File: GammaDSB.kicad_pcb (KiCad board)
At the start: 2 copper layers, 85 x 50 mm, 75 parts, among them J1 AudioIn, J2 AudioOut, J3 Conn_Coaxial, J4 Barrel_Jack, K1 G5V-2, Q1 BC-817, Q2 BC-817, Q3 BC-817, Q4 BC-817, Q5 C1162, Q6 BC817, Q7 BC-817, Q8 BC-817, T1 FT37-43 BIF8T, U1 MCP1700-5002E_SOT89, U2 NE602, Y1 7074, Y2 7074

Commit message: Small improvements.
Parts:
- Q6: value BC817 -> BC807
- moved C25 12.4 mm to (198.2, 108.4), turned to 90 degrees
- moved C10 6.07 mm to (151.7, 111.0), turned to 0 degrees
- moved C5 3.98 mm to (157.3, 109.5), turned to 270 degrees
- moved R17 3.84 mm to (151.2, 118.0), turned to 180 degrees
- moved C14 3.58 mm to (154.2, 98.2), turned to 0 degrees
- moved R21 2.20 mm to (161.6, 117.7)
- moved Y1 2.00 mm to (160.8, 106.0)
- moved R3 1.93 mm to (156.8, 101.0)
- moved D3 1.60 mm to (158.7, 116.0)
- moved C26 1.20 mm to (148.6, 114.2)
- moved Q2 0.40 mm to (154.1, 101.0)
- moved C8 0.36 mm to (157.3, 106.3)
- moved Q6 0.20 mm to (155.6, 117.2)
- moved C28 0.10 mm to (163.3, 114.3)
- moved Q7 0.10 mm to (166.7, 115.1)
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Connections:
- C5 pad 1: Net-(C10-Pad2) -> Net-(C5-Pad1)
- R16 pad 2: Net-(R16-Pad2) -> +12V
- R19 pad 2: Net-(R16-Pad2) -> +12V
- R20 pad 2: Net-(R16-Pad2) -> +12V
- U2 pad 1: Net-(C10-Pad2) -> Net-(C5-Pad1)
- Y1 pad 1: Net-(C10-Pad2) -> Net-(C5-Pad1)
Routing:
- net +12V: track 126.6 -> 168.9 mm
- net Net-(C5-Pad1): track 0.00 -> 7.14 mm
- net Net-(C10-Pad1): track 29.7 -> 23.3 mm
- net Net-(C10-Pad2): track 12.7 -> 7.83 mm
- net Net-(C14-Pad1): track 21.1 -> 16.7 mm
- net Net-(R16-Pad2): track 3.42 -> 0.00 mm
- net Net-(K1-Pad11): track 21.3 -> 23.1 mm
- net Net-(C25-Pad2): track 17.6 -> 19.1 mm
- net /VccR: track 27.5 -> 28.4 mm
- net /VccT: track 49.1 -> 50.0 mm
- net Net-(C28-Pad1): track 58.2 -> 57.4 mm
- net Net-(C28-Pad2): track 6.31 -> 5.63 mm
- net GND: track 78.2 -> 78.1 mm, vias 100 -> 102

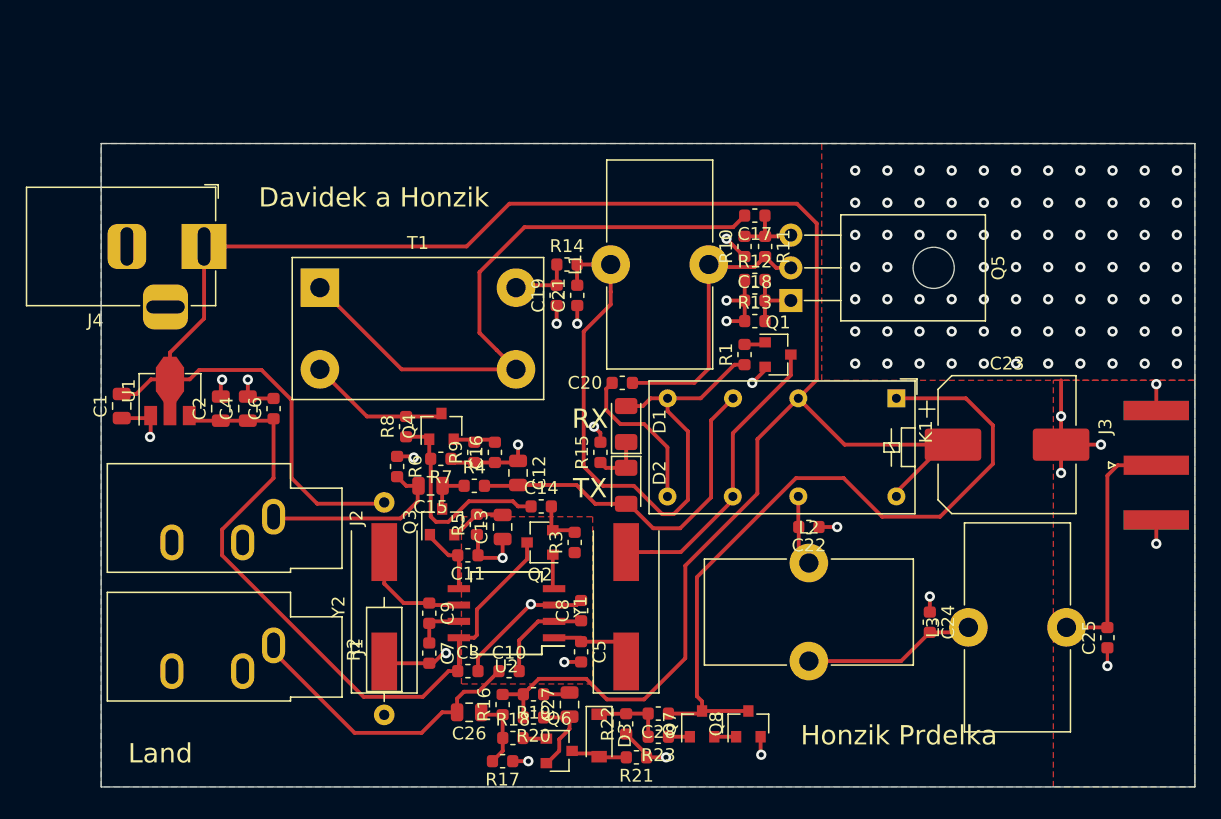
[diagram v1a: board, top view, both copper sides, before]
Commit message: Changed L1 and T1 footprints
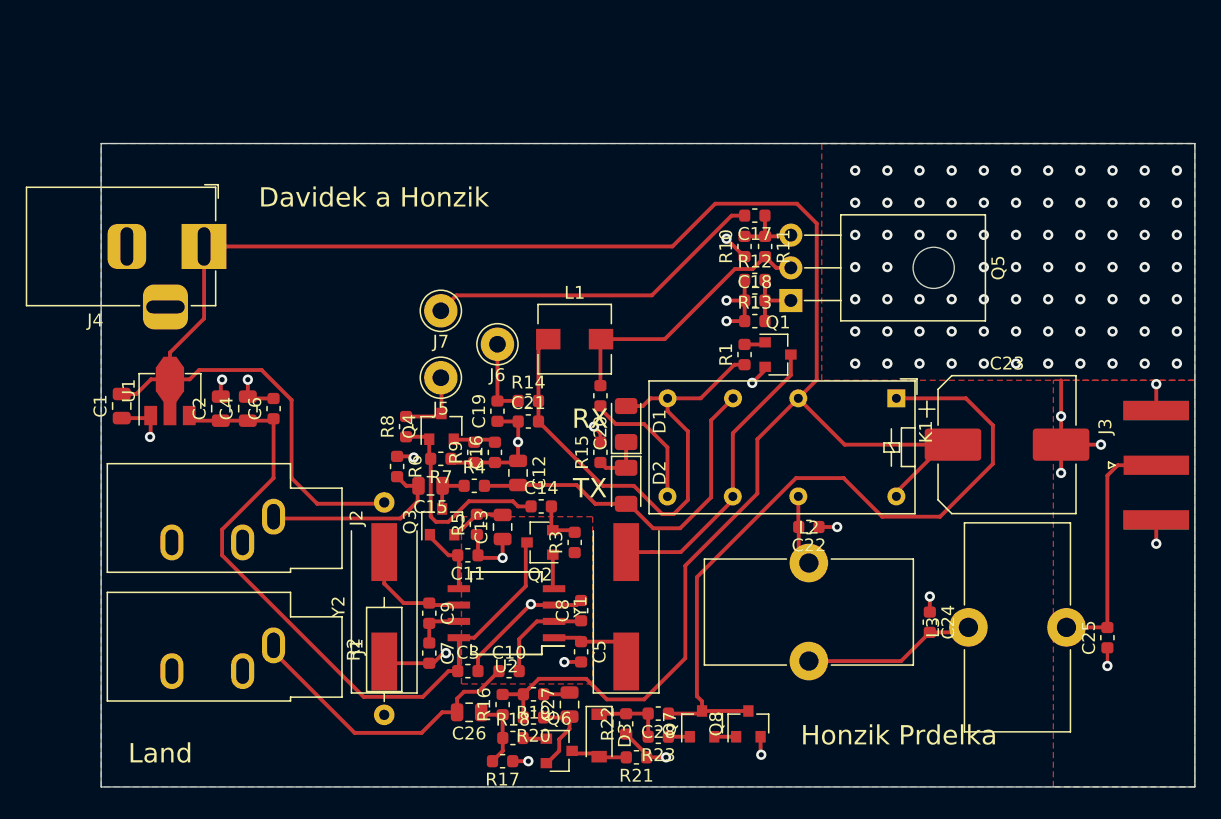
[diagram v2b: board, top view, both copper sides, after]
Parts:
- removed T1: FT37-43 BIF8T, Inductor_THT:L_CommonMode_Toroid_Vertical_L19.3mm_W10.8mm_Px6.35mm_Py15.24mm_Bourns_8100
- added J5: Conn_01x01, Connector_Pin:Pin_D1.3mm_L11.0mm, F.Cu at (146.4, 88.2)
- added J6: Conn_01x01, Connector_Pin:Pin_D1.3mm_L11.0mm, F.Cu at (150.8, 85.6)
- added J7: Conn_01x01, Connector_Pin:Pin_D1.3mm_L11.0mm, F.Cu at (146.4, 83.0)
- L1: value FT37-43 8T -> 74437324220; footprint Inductor_THT:L_Toroid_Vertical_L16.0mm_W8.0mm_P7.62mm -> Inductor_SMD:L_Wuerth_HCI-5040
- moved R14 11.0 mm to (153.2, 90.0)
- moved C21 10.5 mm to (153.2, 91.6), turned to 0 degrees
- moved C19 10.1 mm to (150.8, 90.8)
- moved L1 6.44 mm to (156.8, 85.2), turned to 0 degrees
- moved C20 1.97 mm to (158.8, 89.6), turned to 270 degrees
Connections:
- J1 pad T: Net-(J1-PadT) -> (no net)
- J2 pad T: Net-(J2-PadT) -> (no net)
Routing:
- net Net-(C17-Pad2): track 49.0 -> 26.7 mm
- net /VccT: track 50.0 -> 40.9 mm
- net Net-(J5-Pad1): track 11.1 -> 5.65 mm
- net Net-(C20-Pad2): track 12.3 -> 10.7 mm
- net Net-(C19-Pad2): track 4.86 -> 6.03 mm
- net GND: track 78.1 -> 78.7 mm, vias 102 -> 100

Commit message: Changed layout, removed filter, smaller PCB size.
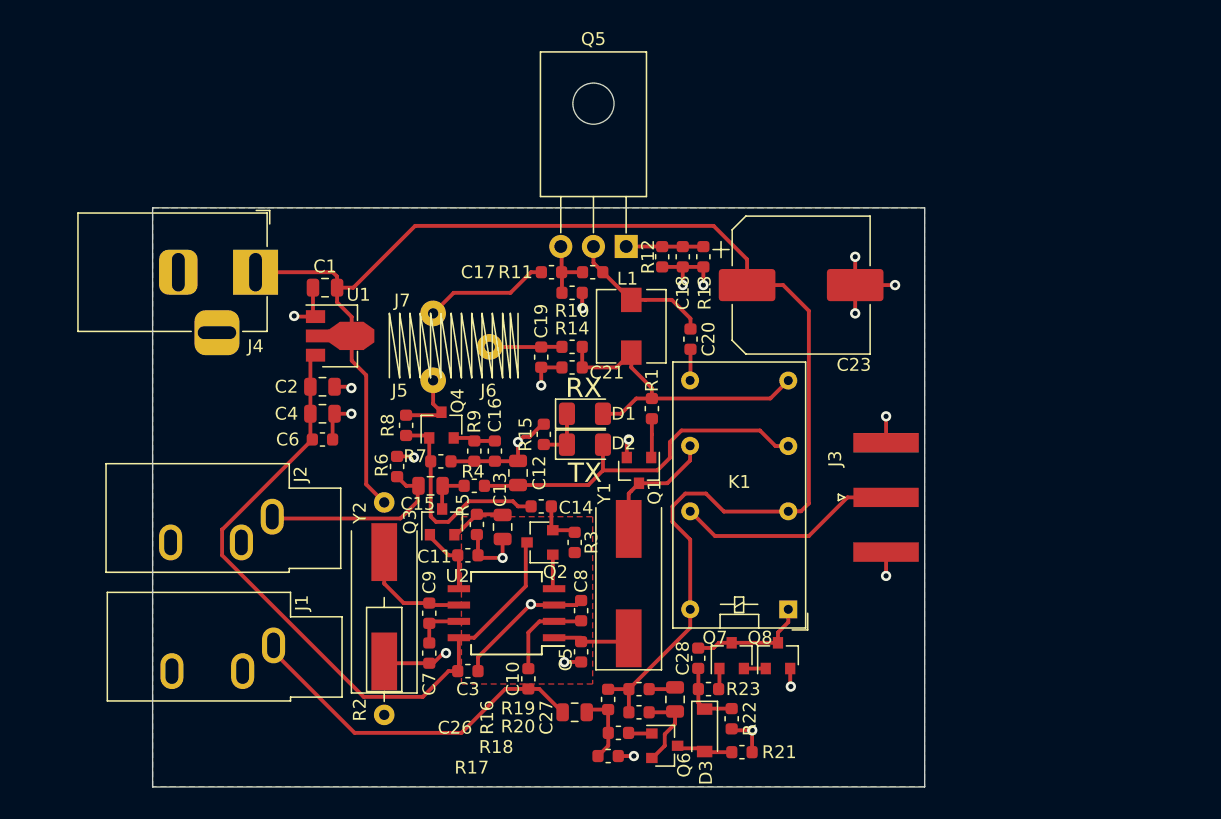
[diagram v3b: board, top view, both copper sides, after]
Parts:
- removed C22, C24, C25: 100n, Capacitor_SMD:C_0603_1608Metric
- removed L2, L3: L, Inductor_THT:L_Toroid_Vertical_L16.0mm_W8.0mm_P7.62mm
- J5, J6, J7: footprint Connector_Pin:Pin_D1.3mm_L11.0mm -> Connector_Wire:SolderWirePad_1x01_Drill0.8mm
- moved J3 21.1 mm to (181.0, 97.5)
- moved C23 20.2 mm to (174.4, 81.0)
- moved K1 18.4 mm to (173.4, 106.2), turned to 180 degrees
- moved C1 18.3 mm to (137.4, 81.2), turned to 0 degrees
- moved C17 16.4 mm to (155.0, 80.0)
- moved Q1 14.1 mm to (161.8, 95.4), turned to 270 degrees
- moved R10 13.9 mm to (156.6, 81.6), turned to 180 degrees
- moved U1 13.6 mm to (138.1, 85.0), turned to 0 degrees
- moved R11 13.5 mm to (158.2, 80.0), turned to 0 degrees
- moved Q5 13.5 mm to (160.8, 78.0), turned to 180 degrees
- moved R1 8.34 mm to (162.8, 90.6), turned to 270 degrees
- moved C20 8.27 mm to (165.8, 85.2)
- moved D3 8.21 mm to (166.9, 115.6)
- moved Q6 8.21 mm to (163.8, 116.8)
- moved R16 8.21 mm to (159.4, 113.2)
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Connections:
- J1 pad T: (no net) -> Net-(J1-PadT)
- J2 pad T: (no net) -> Net-(J2-PadT)
- J3 pad 1: Net-(C25-Pad2) -> Net-(J3-Pad1)
- J4 pad 3: (no net) -> Net-(J4-Pad3)
- K1 pad 13: Net-(C22-Pad2) -> Net-(J3-Pad1)
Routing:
- net +12V: track 168.9 -> 119.1 mm
- net Net-(C28-Pad1): track 57.4 -> 9.30 mm
- net Net-(C25-Pad2): track 19.1 -> 0.00 mm
- net Net-(J3-Pad1): track 0.00 -> 17.3 mm
- net Net-(C17-Pad2): track 26.7 -> 9.74 mm
- net /VccT: track 40.9 -> 25.6 mm
- net Net-(C24-Pad2): track 13.5 -> 0.00 mm
- net Net-(K1-Pad11): track 23.1 -> 9.72 mm
- net Net-(C20-Pad1): track 21.4 -> 11.4 mm
- net Net-(C20-Pad2): track 10.7 -> 2.43 mm
- net GND: track 78.7 -> 71.0 mm, vias 100 -> 22
- net Net-(C22-Pad2): track 5.52 -> 0.00 mm
- net Net-(C10-Pad1): track 23.3 -> 27.7 mm
- net Net-(C18-Pad2): track 5.46 -> 6.85 mm
- net Net-(Q1-Pad1): track 1.67 -> 3.03 mm
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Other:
- board size 85 x 50 mm -> 60 x 45 mm
- board text removed: "Land"
